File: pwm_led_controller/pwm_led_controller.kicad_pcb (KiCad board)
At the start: 2 copper layers, 55.9 x 138.4 mm, 79 parts, among them J1 Conn_01x06_Male, J10 Conn_01x02_Male, J11 Conn_01x02_Male, J12 Conn_01x08_Male, J2 Conn_01x09_Male, J3 Conn_01x02_Male, J4 Conn_01x08_Male, J5 Conn_01x02_Male, J6 Conn_01x02_Male, J7 Conn_01x02_Male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

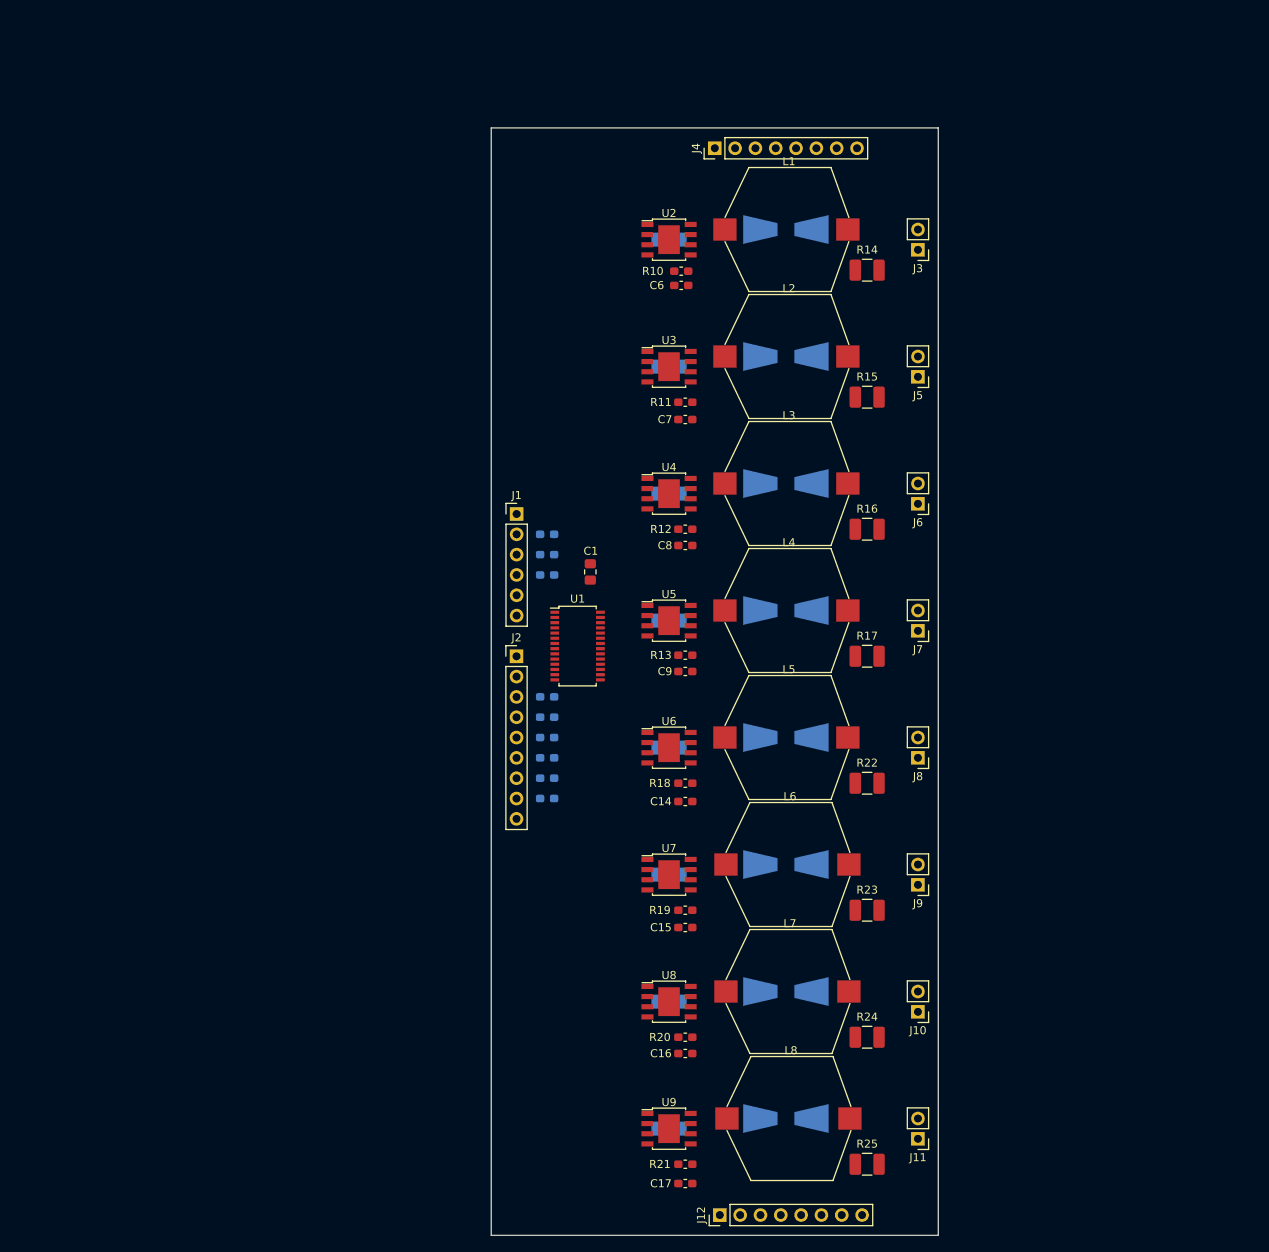
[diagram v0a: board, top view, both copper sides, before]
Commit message: Разведена силовая часть
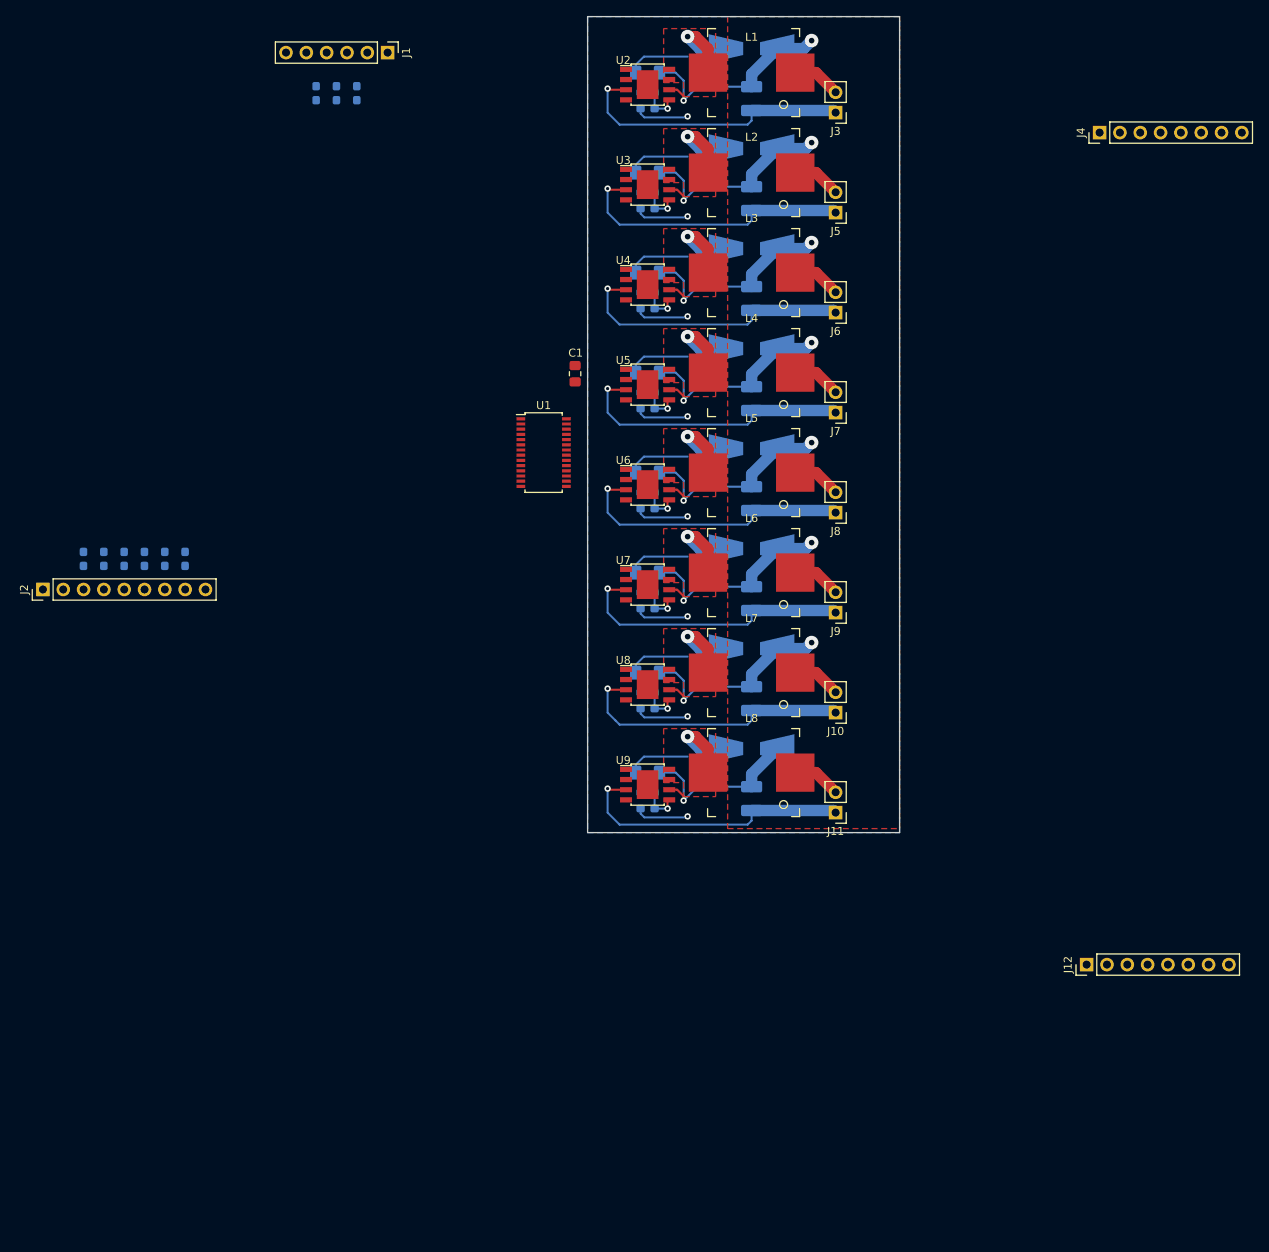
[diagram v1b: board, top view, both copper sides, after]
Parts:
- C14, C15, C16, C17, C6, C7, C8, C9, R10, R11, R12, R13, R14, R15, R16, R17, R18, R19, R20, R21, R22, R23, R24, R25: moved to B.Cu
- L1, L2, L3, L4, L5, L6, L7, L8: footprint my_lib:L_Vishay_IDCS-7328 -> my_lib:Package_2-smd_10.7x10mm
- moved R3 66.8 mm to (61.6, 22.6), turned to 90 degrees
- moved R2 63.4 mm to (64.1, 22.6), turned to 90 degrees
- moved R4 60.5 mm to (32.5, 80.8), turned to 90 degrees
- moved R1 60.1 mm to (66.6, 22.6), turned to 90 degrees
- moved J1 59.9 mm to (70.5, 17.5), turned to 270 degrees
- moved J2 59.8 mm to (27.4, 84.6), turned to 90 degrees
- moved R5 58.8 mm to (35.0, 80.8), turned to 90 degrees
- moved R6 57.4 mm to (37.6, 80.8), turned to 90 degrees
- moved R7 56.1 mm to (40.1, 80.8), turned to 90 degrees
- moved J12 55.5 mm to (157.9, 131.5)
- moved R8 55.1 mm to (42.6, 80.8), turned to 90 degrees
- moved R9 54.3 mm to (45.2, 80.8), turned to 90 degrees
- moved J4 48.1 mm to (159.5, 27.5)
- moved R25 47.9 mm to (116.0, 110.8), turned to 90 degrees
- moved C17 47.1 mm to (103.0, 112.0)
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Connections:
- J12 pad 1: GND -> +48V
- J12 pad 2: GND -> +48V
- J12 pad 3: GND -> +48V
- J12 pad 4: GND -> +48V
- J4 pad 5: +48V -> GND
- J4 pad 6: +48V -> GND
- J4 pad 7: +48V -> GND
- J4 pad 8: +48V -> GND
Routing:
- net +48V: track 0.00 -> 223.8 mm, vias 0 -> 15
- net GND: track 0.00 -> 115.8 mm, vias 0 -> 8
- net /Set_7: track 0.00 -> 36.1 mm, vias 0 -> 1
- net /Set_6: track 0.00 -> 36.1 mm, vias 0 -> 1
- net /Set_5: track 0.00 -> 36.1 mm, vias 0 -> 1
- net /Set_4: track 0.00 -> 36.1 mm, vias 0 -> 1
- net /Set_0: track 0.00 -> 36.1 mm, vias 0 -> 1
- net /Set_3: track 0.00 -> 36.1 mm, vias 0 -> 1
- net /Set_1: track 0.00 -> 36.1 mm, vias 0 -> 1
- net /Set_2: track 0.00 -> 36.1 mm, vias 0 -> 1
- net /SW_7: track 0.00 -> 11.6 mm, vias 0 -> 1
- net /SW_6: track 0.00 -> 11.6 mm, vias 0 -> 1
- net /SW_5: track 0.00 -> 11.6 mm, vias 0 -> 1
- net /SW_4: track 0.00 -> 11.6 mm, vias 0 -> 1
- net /SW_3: track 0.00 -> 11.6 mm, vias 0 -> 1
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- added copper zone on F.Cu, net +48V
- added copper zone on F.Cu, net /SW_0
- added copper zone on F.Cu, net /SW_1
- added copper zone on F.Cu, net /SW_2
- added copper zone on F.Cu, net /SW_3
- added copper zone on F.Cu, net /SW_4
- added copper zone on F.Cu, net /SW_5
- added copper zone on F.Cu, net /SW_6
- added copper zone on F.Cu, net /SW_7
- added copper zone on B.Cu, net GND
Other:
- board size 55.9 x 138.4 mm -> 39 x 102 mm
- net class Default: clearance 0.2 -> 0.5
- net class POWER added: clearance 0.5, trace_width 1.425, via_dia 1.7, via_drill 0.7
- rule trace_clearance: 0.2 -> 0.5

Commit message: Закончена трассировка
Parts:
- C1: moved to B.Cu
- moved R3 74.1 mm to (95.5, 88.5), turned to 180 degrees
- moved R4 71.2 mm to (95.5, 114.0), turned to 0 degrees
- moved R2 70.8 mm to (95.5, 86.0), turned to 180 degrees
- moved R5 70.2 mm to (95.5, 116.5), turned to 0 degrees
- moved R6 69.4 mm to (95.5, 119.1), turned to 0 degrees
- moved R7 68.8 mm to (95.5, 121.6), turned to 0 degrees
- moved J2 68.6 mm to (91.5, 109.0), turned to 0 degrees
- moved R8 68.4 mm to (95.5, 124.1), turned to 0 degrees
- moved R9 68.1 mm to (95.5, 126.7), turned to 0 degrees
- moved R1 67.4 mm to (95.5, 83.5), turned to 180 degrees
- moved J1 66.9 mm to (91.5, 81.0), turned to 0 degrees
- moved C1 43.4 mm to (92.8, 101.0), turned to 270 degrees
- moved J4 42.7 mm to (142.0, 66.4), turned to 0 degrees
- moved C10 37.3 mm to (108.0, 107.0)
- moved C11 37.3 mm to (108.0, 119.5)
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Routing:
- net /PWM_7: track 0.00 -> 51.8 mm, vias 0 -> 1
- net VSS: track 0.00 -> 51.3 mm, vias 0 -> 1
- net /PWM_0: track 0.00 -> 50.1 mm, vias 0 -> 1
- net VDD: track 0.00 -> 42.0 mm, vias 0 -> 1
- net /PWM_6: track 0.00 -> 40.1 mm, vias 0 -> 1
- net /PWM_1: track 0.00 -> 37.4 mm, vias 0 -> 1
- net /A5: track 0.00 -> 33.6 mm
- net /PWM_5: track 0.00 -> 27.0 mm, vias 0 -> 1
- net /CLK: track 0.00 -> 25.5 mm, vias 0 -> 1
- net /A4: track 0.00 -> 25.1 mm, vias 0 -> 1
- net /PWM_2: track 0.00 -> 24.7 mm, vias 0 -> 1
- net /A3: track 0.00 -> 22.5 mm, vias 0 -> 1
- net /A2: track 0.00 -> 19.8 mm, vias 0 -> 1
- net /SCL: track 0.00 -> 18.9 mm, vias 0 -> 1
- net /A1: track 0.00 -> 17.2 mm, vias 0 -> 1
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- added copper zone on F.Cu, net GND
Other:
- board size 39 x 102 mm -> 55 x 110 mm
- net class Default: clearance 0.5 -> 0.2
- rule trace_clearance: 0.5 -> 0.2
